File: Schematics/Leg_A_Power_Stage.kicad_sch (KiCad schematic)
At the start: 40 parts, among them Q2 C3M0025065K, Q3 C3M0025065K, U1 UCC21710QDWRQ1, U2 UCC21710QDWRQ1

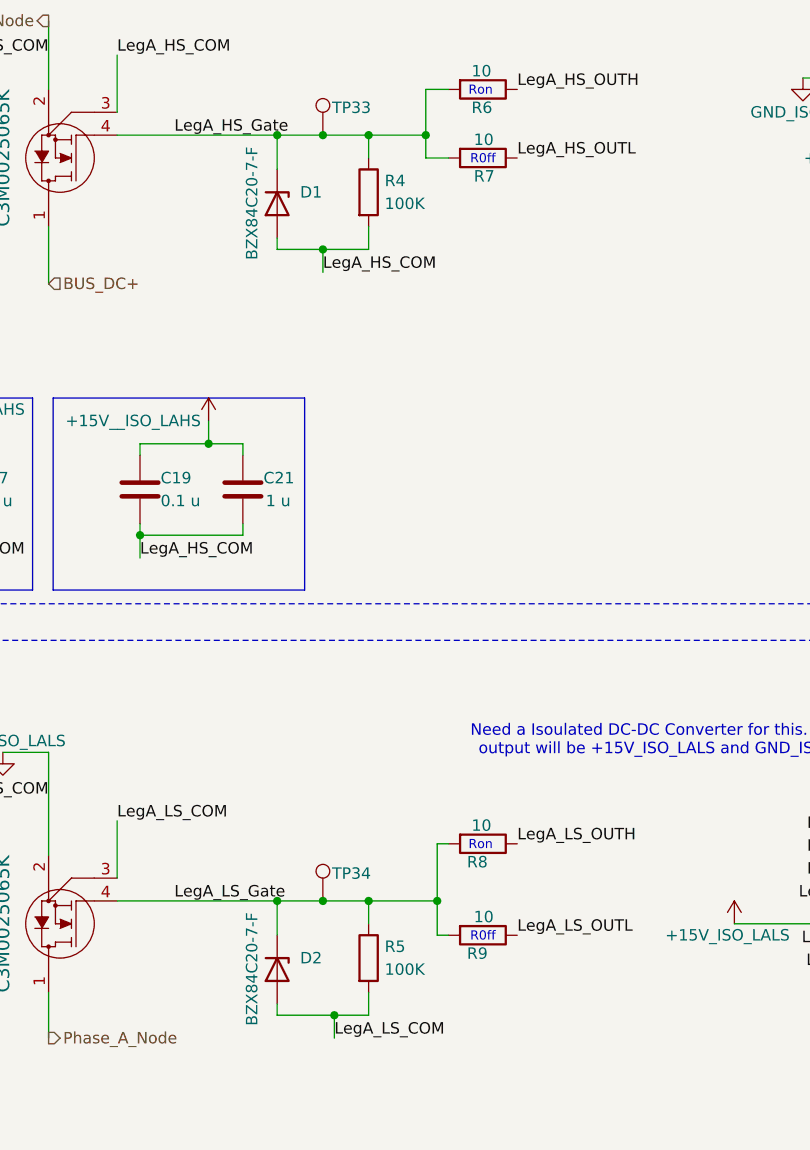
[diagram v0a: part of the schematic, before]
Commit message: [WIP Input Protection Circuit to Controller]
- Added Gate node input protection pin to controller
- Added optocoupler to input protection circuit
- Added 3d model for PC817.....
- Updated PCB to test out PCB modularity
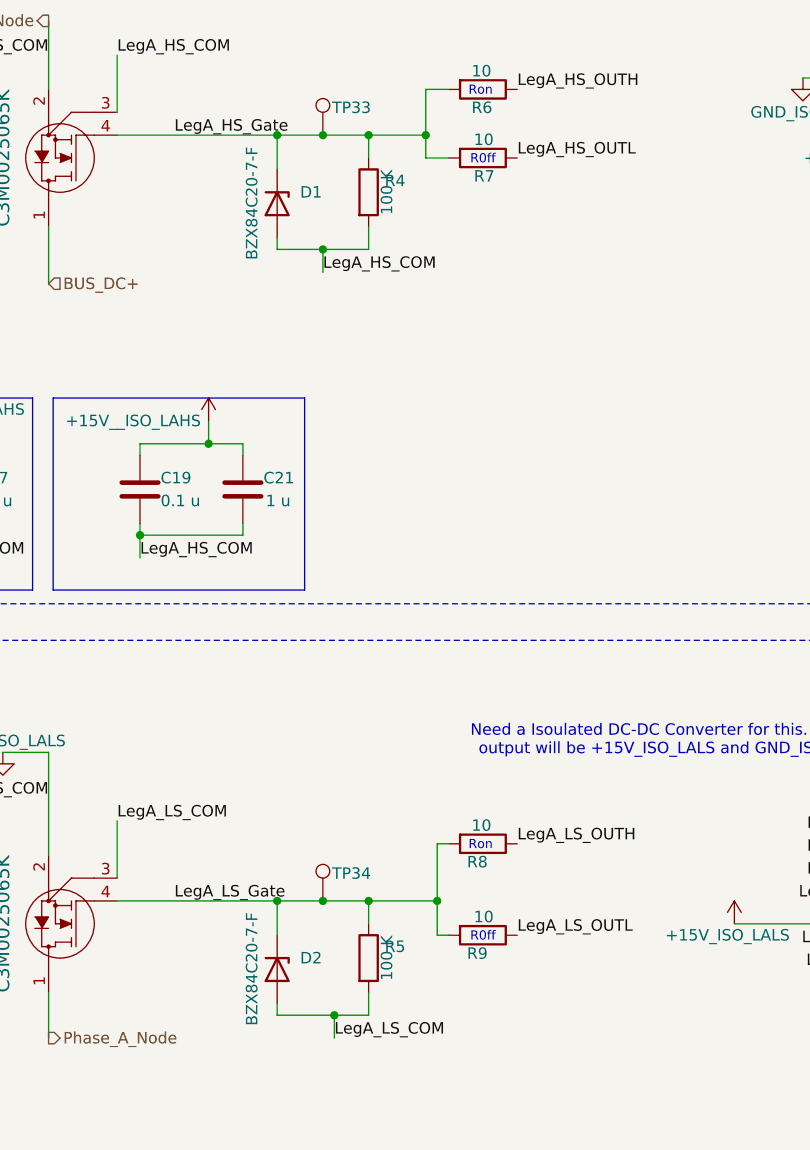
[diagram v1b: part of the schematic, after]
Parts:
- R4, R5: value 100K -> 100 K; symbol Device:R -> SiC_Inverter:RT1206BRD07100KL
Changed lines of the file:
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@@
 	)
 	(symbol
-		(lib_id "Device:R")
+		(lib_id "SiC_Inverter:RT1206BRD07100KL")
 		(at 71.12 147.32 0)
 		(unit 1)
@@
 			)
 		)
-		(property "Value" "100K"
-			(at 72.898 148.59 0)
-			(effects
-				(font
-					(size 1.27 1.27)
-				)
-				(justify left)
+		(property "Value" "100 K"
+			(at 73.152 147.32 90)
+			(effects
+				(font
+					(size 1.27 1.27)
+				)
 			)
 		)
 		(property "Footprint" "Resistor_SMD:R_1206_3216Metric_Pad1.30x1.75mm_HandSolder"
-			(at 69.342 147.32 90)
-			(effects
-				(font
-					(size 1.27 1.27)
-				)
-				(hide yes)
-			)
-		)
-		(property "Datasheet" "~"
-			(at 71.12 147.32 0)
-			(effects
-				(font
-					(size 1.27 1.27)
-				)
-				(hide yes)
-			)
-		)
-		(property "Description" "Resistor"
-			(at 71.12 147.32 0)
+			(at 84.074 158.75 0)
+			(effects
+				(font
+					(size 1.27 1.27)
+				)
+				(hide yes)
+			)
+		)
+		(property "Datasheet" "https://www.mouser.com/datasheet/3/508/1/PYu-RT_1-to-0.01_RoHS_L_15.pdf"
+			(at 93.472 161.036 0)
+			(effects
+				(font
+					(size 1.27 1.27)
+				)
+				(hide yes)
+			)
+		)
+		(property "Description" "Thin Film Resistors - SMD 1/4W 5K ohm .1% 25ppm"
+			(at 79.756 163.322 0)
 			(effects
 				(font
@@
 	)
 	(symbol
-		(lib_id "Device:R")
+		(lib_id "SiC_Inverter:RT1206BRD07100KL")
 		(at 71.12 62.23 0)
 		(unit 1)
@@
 			)
 		)
-		(property "Value" "100K"
-			(at 72.898 63.5 0)
-			(effects
-				(font
-					(size 1.27 1.27)
-				)
-				(justify left)
+		(property "Value" "100 K"
+			(at 73.152 62.23 90)
+			(effects
+				(font
+					(size 1.27 1.27)
+				)
 			)
 		)
 		(property "Footprint" "Resistor_SMD:R_1206_3216Metric_Pad1.30x1.75mm_HandSolder"
-			(at 69.342 62.23 90)
-			(effects
-				(font
-					(size 1.27 1.27)
-				)
-				(hide yes)
-			)
-		)
-		(property "Datasheet" "~"
-			(at 71.12 62.23 0)
-			(effects
-				(font
-					(size 1.27 1.27)
-				)
-				(hide yes)
-			)
-		)
-		(property "Description" "Resistor"
-			(at 71.12 62.23 0)
-			(effects
-				(font
+			(at 84.074 73.66 0)
+			(effects
+				(font
+					(size 1.27 1.27)
+				)
+				(hide yes)
+			)
+		)
+		(property "Datasheet" "https://www.mouser.com/datasheet/3/508/1/PYu-RT_1-to-0.01_RoHS_L_15.pdf"
+			(at 93.472 75.946 0)
+			(effects
+				(font
+					(size 1.27 1.27)
+				)
+				(hide yes)
+			)
+		)
+		(property "Description" "Thin Film Resistors - SMD 1/4W 5K ohm .1% 25ppm"
+			(at 79.756 78.232 0)
+			(effects
+				(font

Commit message: WIP PCB, Added Test Points, added icon file
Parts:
- renumbered D1 to D2, D2 to D3, R9 to R10, R10 to R11, R11 to R12, R12 to R13, R13 to R14, R14 to R15, R15 to R16, R16 to R17, R17 to R18, R4 to R5, R5 to R6, R6 to R7, R7 to R8, R8 to R9, TP33 to TP34, TP34 to TP35
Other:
- moved on the sheet: TP34, TP35

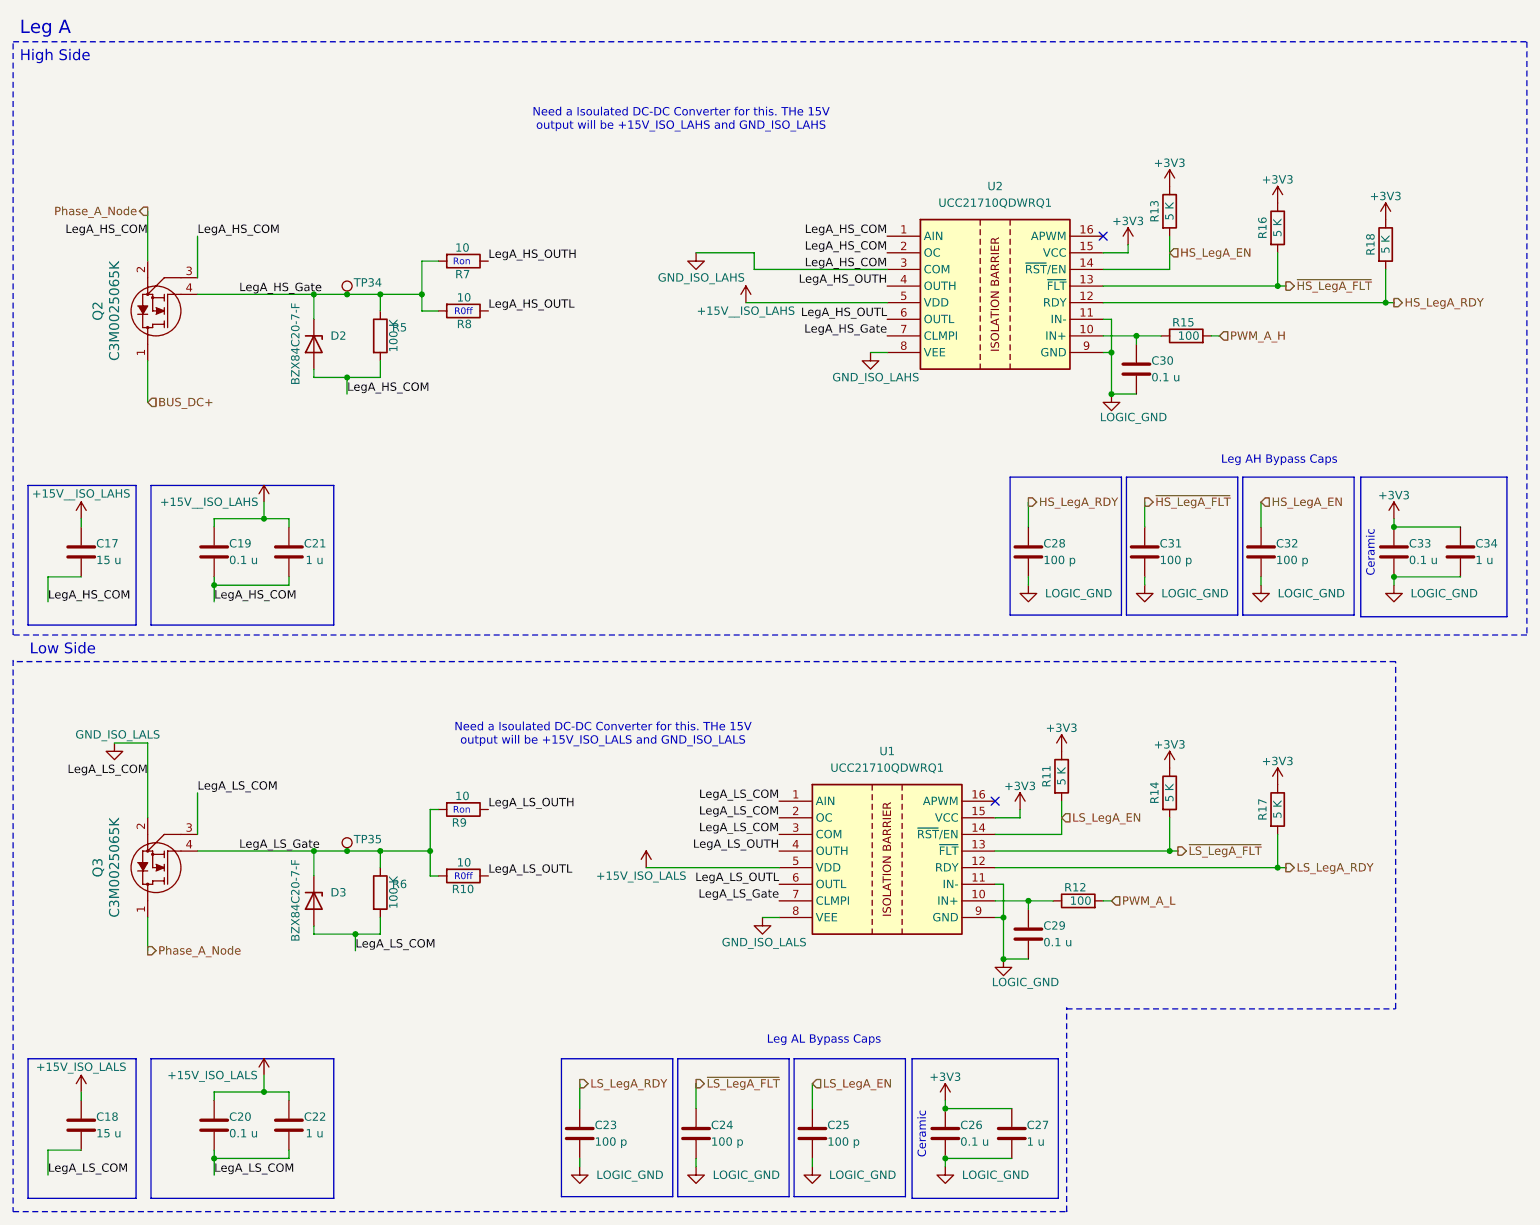
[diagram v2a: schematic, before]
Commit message: Changing units on all Caps to display xF
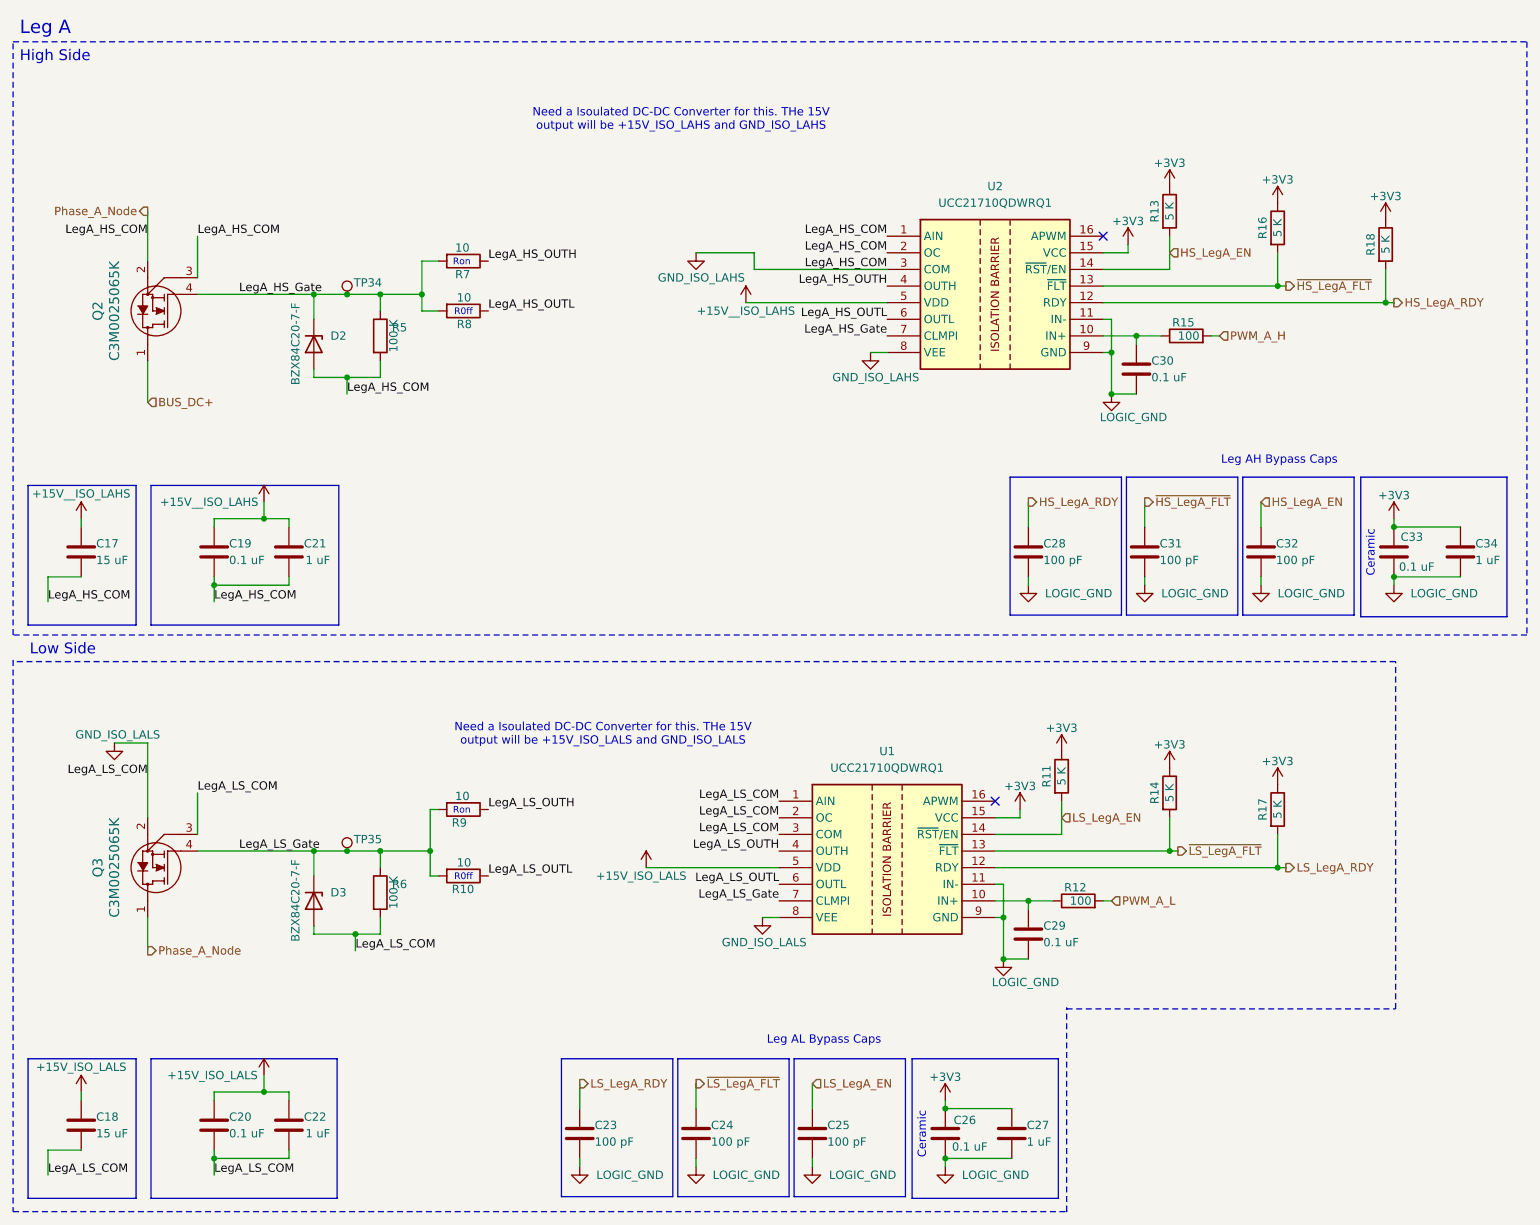
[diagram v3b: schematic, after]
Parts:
- C17, C18: value 15 u -> 15 uF
- C19, C20, C26, C29, C30, C33: value 0.1 u -> 0.1 uF
- C21, C22, C27, C34: value 1 u -> 1 uF
- C23, C24, C25, C28, C31, C32: value 100 p -> 100 pF
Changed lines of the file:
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@@
 	(rectangle
 		(start 36.068 85.09)
-		(end 64.008 106.426)
+		(end 64.77 106.426)
 		(stroke
 			(width 0)
@@
 	(rectangle
 		(start 36.068 172.72)
-		(end 64.008 194.056)
+		(end 64.516 194.056)
 		(stroke
 			(width 0)
@@
 			)
 		)
-		(property "Value" "100 p"
+		(property "Value" "100 pF"
 			(at 172.466 96.52 0)
 			(effects
@@
 			)
 		)
-		(property "Value" "100 p"
+		(property "Value" "100 pF"
 			(at 139.446 185.42 0)
 			(effects
@@
 			)
 		)
-		(property "Value" "0.1 u"
+		(property "Value" "0.1 uF"
 			(at 172.466 154.94 0)
 			(effects
@@
 			)
 		)
-		(property "Value" "1 u"
+		(property "Value" "1 uF"
 			(at 169.926 185.42 0)
 			(effects
@@
 			)
 		)
-		(property "Value" "0.1 u"
+		(property "Value" "0.1 uF"
 			(at 48.006 184.15 0)
 			(effects
@@
 			)
 		)
-		(property "Value" "100 p"
+		(property "Value" "100 pF"
 			(at 121.666 185.42 0)
 			(effects
@@
 			)
 		)
-		(property "Value" "15 u"
+		(property "Value" "15 uF"
 			(at 27.686 184.15 0)
 			(effects
@@
 			)
 		)
-		(property "Value" "15 u"
+		(property "Value" "15 uF"
 			(at 27.686 96.52 0)
 			(effects
@@
 			)
 		)
-		(property "Value" "1 u"
+		(property "Value" "1 uF"
 			(at 59.69 96.52 0)
 			(effects
@@
 		(dnp no)
 		(property "Reference" "C33"
-			(at 228.346 93.98 0)
+			(at 227.076 92.964 0)
 			(effects
 				(font
@@
 			)
 		)
-		(property "Value" "0.1 u"
-			(at 228.346 96.52 0)
+		(property "Value" "0.1 uF"
+			(at 226.822 97.536 0)
 			(effects
 				(font
@@
 		(dnp no)
 		(property "Reference" "C26"
-			(at 159.766 182.88 0)
+			(at 158.75 182.118 0)
 			(effects
 				(font
@@
 			)
 		)
-		(property "Value" "0.1 u"
-			(at 159.766 185.42 0)
+		(property "Value" "0.1 uF"
+			(at 158.496 186.182 0)
 			(effects
 				(font
@@
 			)
 		)
-		(property "Value" "100 p"
+		(property "Value" "100 pF"
 			(at 208.026 96.52 0)
 			(effects
@@
 			)
 		)
-		(property "Value" "100 p"
+		(property "Value" "100 pF"
 			(at 103.886 185.42 0)
 			(effects
@@
 			)
 		)
-		(property "Value" "0.1 u"
+		(property "Value" "0.1 uF"
 			(at 48.006 96.52 0)
 			(effects
@@
 			)
 		)
-		(property "Value" "1 u"
+		(property "Value" "1 uF"
 			(at 59.69 184.15 0)
 			(effects
@@
 			)
 		)
-		(property "Value" "1 u"
+		(property "Value" "1 uF"
 			(at 238.506 96.52 0)
 			(effects
@@
 			)
 		)
-		(property "Value" "100 p"
+		(property "Value" "100 pF"
 			(at 190.246 96.52 0)
 			(effects
@@
 			)
 		)
-		(property "Value" "0.1 u"
+		(property "Value" "0.1 uF"
 			(at 188.976 68.58 0)
 			(effects
